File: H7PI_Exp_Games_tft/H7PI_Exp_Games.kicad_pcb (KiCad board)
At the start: 2 copper layers, 65 x 30 mm, 45 parts, among them J1 Header_1x2, K1 KAN0741-0601M1, Q1 CJ2102, Q2 CJ2102, U1 ME6215C33M5G, U10 H7PI_Exp, U11 KLJ-5018, U2 AHT10, U3 BH1730FVC-TR, U4 HP203B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

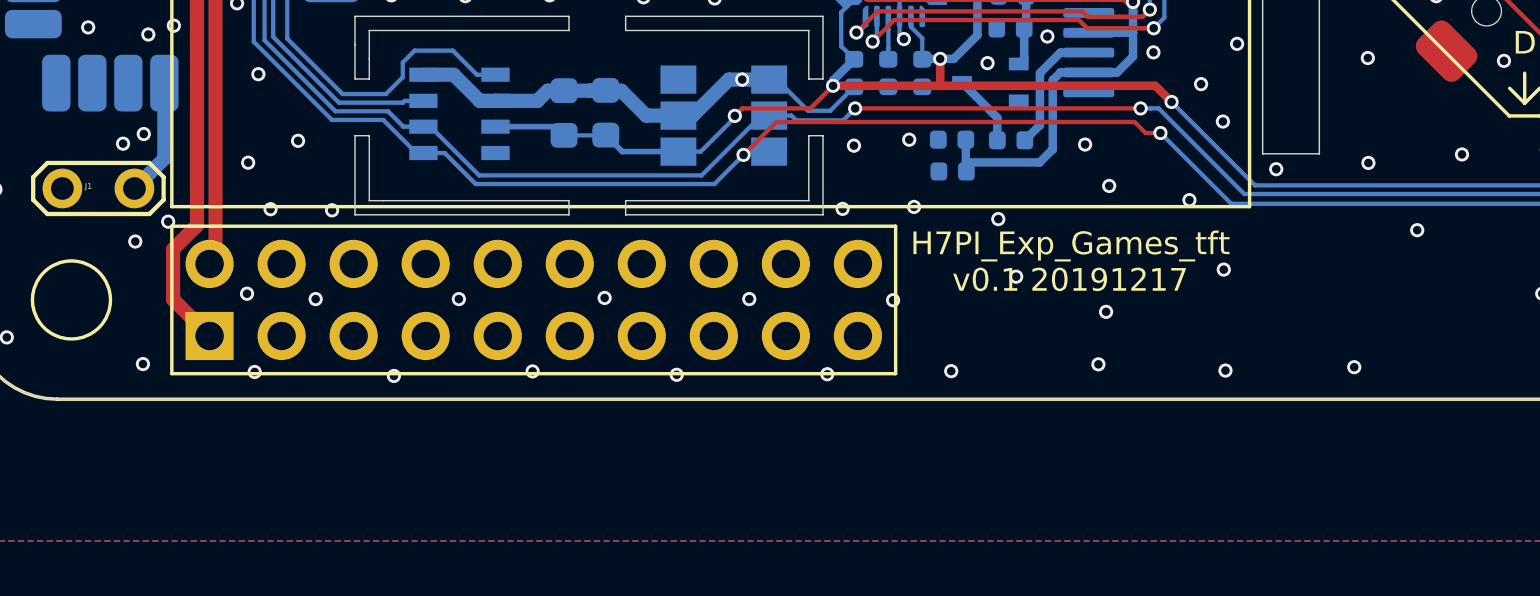
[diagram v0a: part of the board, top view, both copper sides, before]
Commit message: v0.2 update expansion board symbol and footprint
Signed-off-by: fuhua-chen <fuhua-chen@outlook.com>
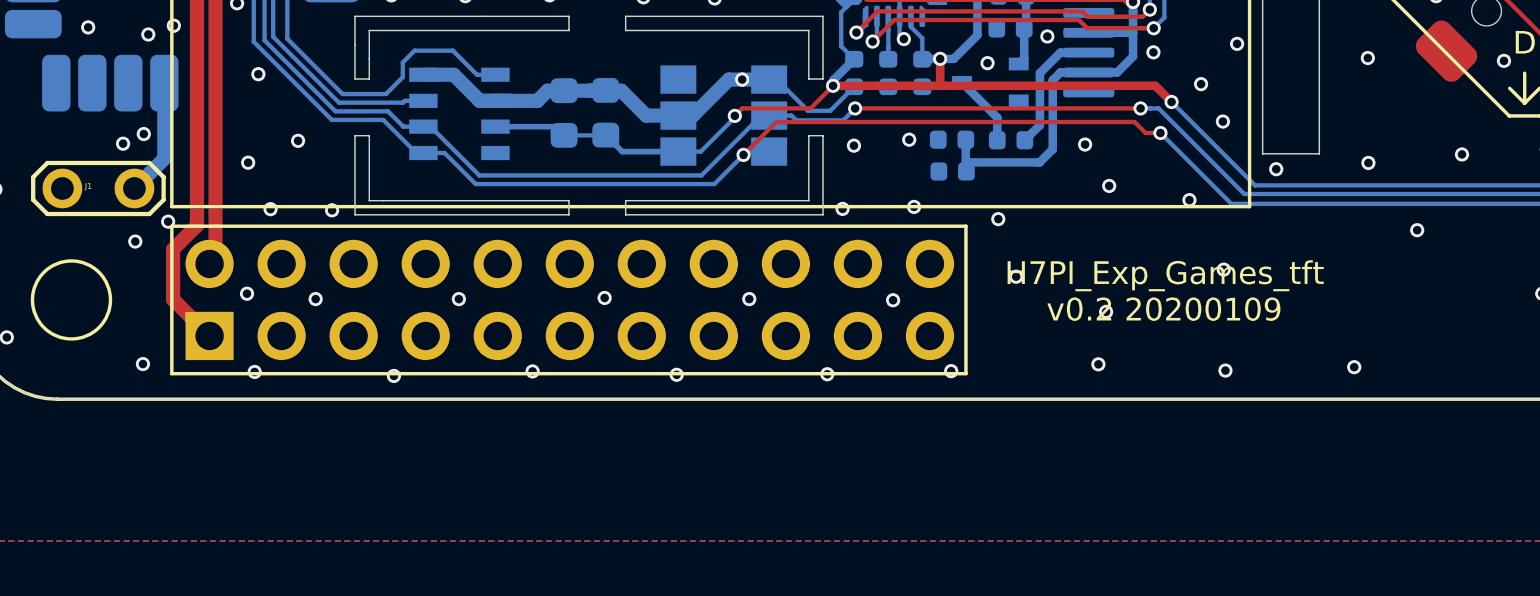
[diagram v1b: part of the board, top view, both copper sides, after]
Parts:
- C1, C10, C11, C2, C22, C3, C9: footprint Capacitor_SMD:C_0603_1608Metric -> C_0603_1608Metric
- C12, C13, C14, C15, C16, C4, C5, C6, C7, C8: footprint Capacitor_SMD:C_0402_1005Metric -> C_0402_1005Metric
- D2: footprint Diode_SMD:D_SOD-323 -> D_SOD-323
- Q1, Q2: footprint Package_TO_SOT_SMD:SOT-323_SC-70 -> SOT-323_SC-70
- R1, R10, R2, R24, R25, R26, R3, R4, R5, R6, R7, R8, R9: footprint Resistor_SMD:R_0402_1005Metric -> R_0402_1005Metric
- U1, U5: footprint Package_TO_SOT_SMD:SOT-23-5 -> SOT-23-5
- U10: footprint Pinno:Module_H7PI_Exp_65x30mm -> Module_H7PI_Exp_65x30mm
- U11: footprint Pinno:Buzzer_KEILKING_KLJ-5018_5X5X1.8mm -> Buzzer_KEILKING_KLJ-5018_5X5X1.8mm
- U2: footprint Pinno:Temperature_Humidity_Sensor_ASAIR_AHT10_4x5x1.6mm -> Temperature_Humidity_Sensor_ASAIR_AHT10_4x5x1.6mm
- U3: footprint Pinno:LightSensor_ROHM_BH1730FVC_WSOF6_2.6X1.6X0.75mm -> LightSensor_ROHM_BH1730FVC_WSOF6_2.6X1.6X0.75mm
- U6: footprint Package_DFN_QFN:QFN-24-1EP_3x3mm_P0.4mm_EP1.75x1.6mm -> QFN-24-1EP_3x3mm_P0.4mm_EP1.75x1.6mm
- U7: footprint Pinno:TFT_ZJY114IPS_1.14Inch_135x240Pixels_17.6x31.0x1.6mm -> TFT_ZJY114IPS_1.14Inch_135x240Pixels_17.6x31.0x1.6mm
- U9: footprint Pinno:Module_Bluetooth_HTCTEK_CORE52_12.5X12.5X2mm -> Module_Bluetooth_HTCTEK_CORE52_12.5X12.5X2mm
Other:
- board text added: "H7PI_Exp_Games_tft v0.2 20200109"
- board text removed: "H7PI_Exp_Games_tft v0.1 20191217"
